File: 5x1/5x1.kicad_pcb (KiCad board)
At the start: 2 copper layers, 95.2 x 19.1 mm, 7 parts, among them J1 Conn_01x10_Male, U1 Elite-C

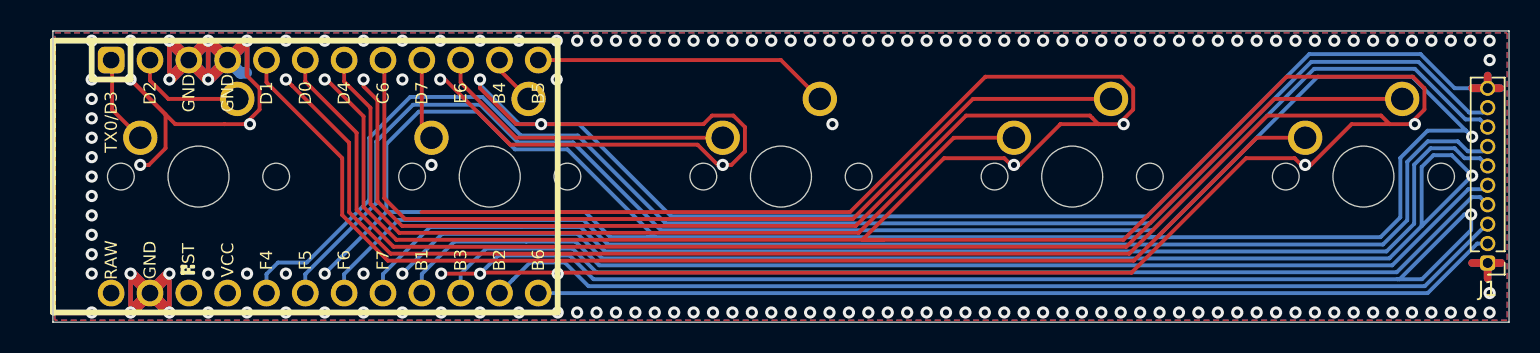
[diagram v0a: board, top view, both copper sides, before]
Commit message: added silkscreen
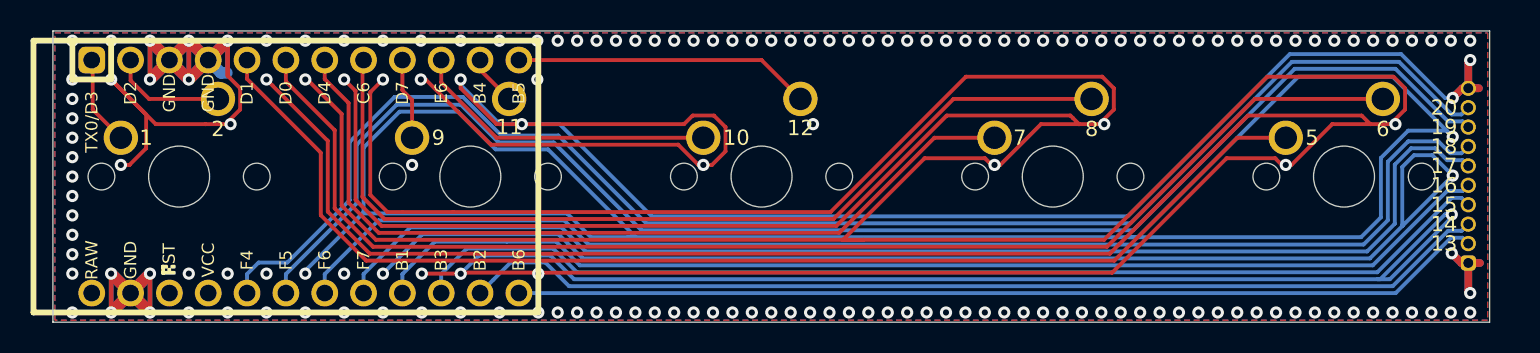
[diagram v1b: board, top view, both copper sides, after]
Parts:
- moved MX_2 1.27 mm to (46.4, 9.53)
- moved MX_0 1.27 mm to (8.26, 9.53)
- moved MX_1 1.27 mm to (27.3, 9.53)
- moved U1 1.27 mm to (16.5, 9.53)
- moved J1 1.27 mm to (92.6, 15.2)
- moved MX_3 1.27 mm to (65.4, 9.53)
- moved MX_4 1.27 mm to (84.5, 9.53)
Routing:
- net GND: track 883.5 -> 899.4 mm, vias 169 -> 171
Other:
- board size 95.2 x 19.1 mm -> 94 x 19.1 mm
- board text added: "1"
- board text added: "10"
- board text added: "11"
- board text added: "12"
- board text added: "13"
- board text added: "14"
- board text added: "15"
- board text added: "16"
- board text added: "17"
- board text added: "18"
- board text added: "19"
- board text added: "2"
- board text added: "20"
- board text added: "5"
- board text added: "6"
- board text added: "7"
- board text added: "8"
- board text added: "9"

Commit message: 5trange dot as built
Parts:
- removed J1: Conn_01x10_Male, Connector_PinHeader_1.27mm:PinHeader_1x10_P1.27mm_Vertical
- removed MX_0: MX-NoLED, MX_Only:MXOnly-1U-NoLED
- added J_0: Conn_01x10_Male, Connector_PinHeader_1.27mm:PinHeader_1x10_P1.27mm_Vertical, F.Cu at (92.6, 3.75)
- added MX_5: MX-NoLED, MX_Only:MXOnly-1U-NoLED, F.Cu at (84.4, 9.53)
- moved MX_1 19.1 mm to (8.19, 9.53)
- moved MX_3 19.1 mm to (46.3, 9.53)
- moved MX_4 19.1 mm to (65.3, 9.53)
- moved MX_2 19.1 mm to (27.2, 9.53)
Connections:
- MX_1 pad 1: C1 -> C0
- MX_1 pad 2: R1 -> R0
- MX_2 pad 1: C2 -> C1
- MX_2 pad 2: R2 -> R1
- MX_3 pad 1: C3 -> C2
- MX_3 pad 2: R3 -> R2
- MX_4 pad 1: C4 -> C3
- MX_4 pad 2: R4 -> R3
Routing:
- net GND: track 899.4 -> 1483.7 mm, vias 171 -> 118
- net Net-(J_0-Pad2): track 97.6 -> 91.7 mm
- net Net-(J_0-Pad3): track 94.8 -> 89.6 mm
- net Net-(J_0-Pad7): track 72.0 -> 70.3 mm
- net Net-(J_0-Pad4): track 83.7 -> 82.1 mm
- net Net-(J_0-Pad5): track 81.0 -> 80.0 mm
- net Net-(J_0-Pad6): track 74.7 -> 74.0 mm
- net Net-(J_0-Pad8): track 67.8 -> 67.3 mm
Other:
- net class Default: clearance 0.2 -> 0.2032; trace_width 0.25 -> 0.254
- rule trace_clearance: 0.2 -> 0.2032
- rule trace_min: 0.2032 -> 0.254
- board text added: "0x02 "5trange""
- board text added: "JLCJLCJLCJLC"

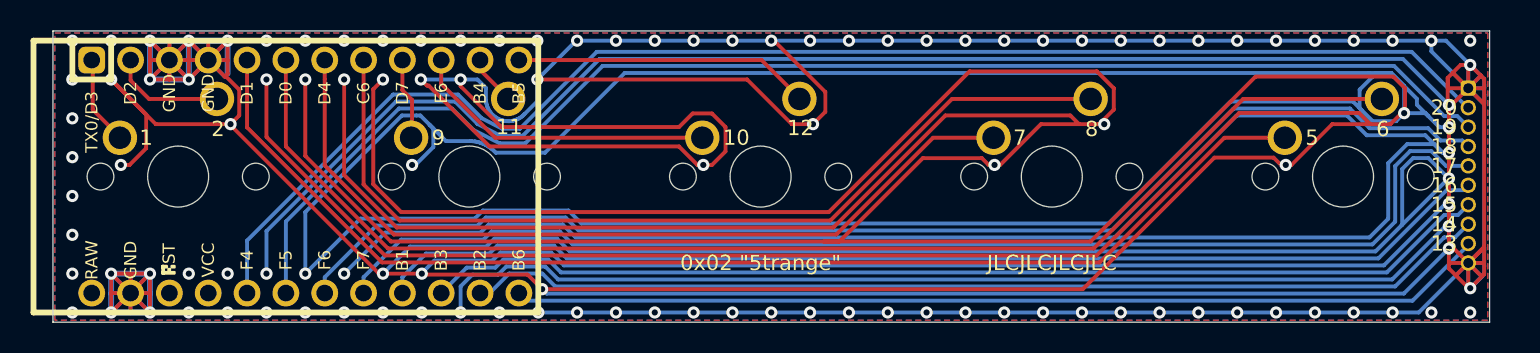
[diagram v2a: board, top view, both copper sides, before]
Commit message: touched up things and detached the case ground and electrical ground on the dot board
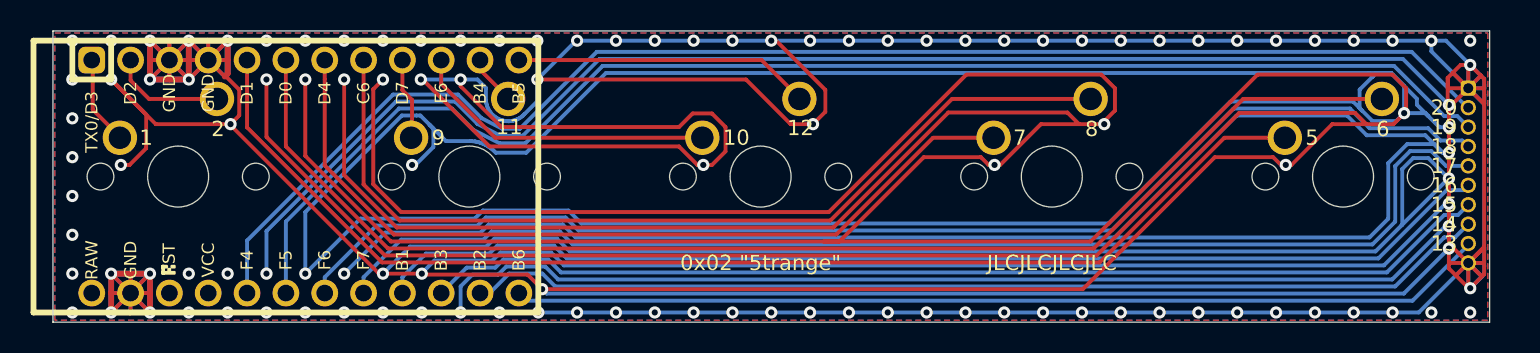
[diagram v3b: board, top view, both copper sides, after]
